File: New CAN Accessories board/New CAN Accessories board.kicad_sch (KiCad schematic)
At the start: 22 parts, among them J10 39301040, J11 ATF13-2P-BM03, J12 Conn_01x02_Pin, J9 39301060, T1 MCP2562FD-E_SN, U1 NUCLEO_L432KC

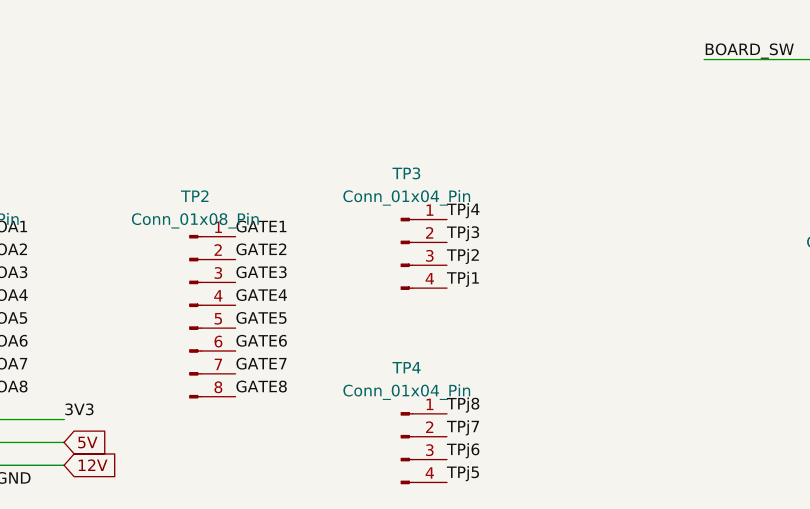
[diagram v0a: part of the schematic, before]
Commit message: added labellling changes noted in design review
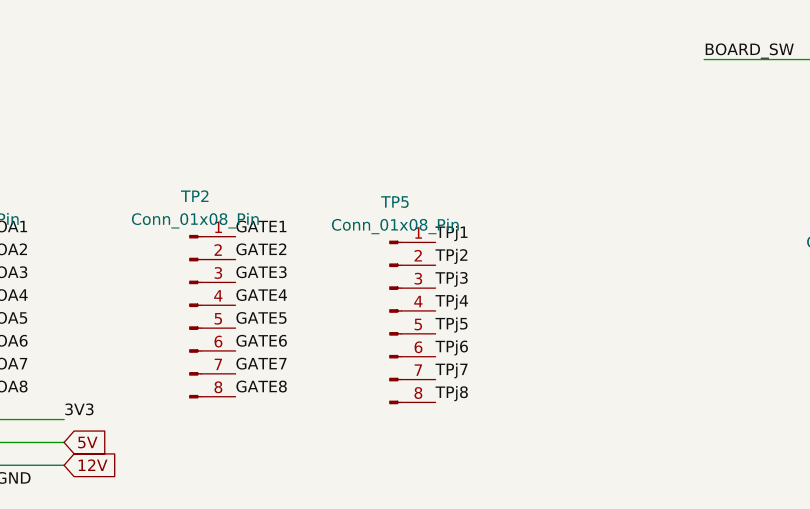
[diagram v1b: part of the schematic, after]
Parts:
- removed TP3, TP4: Conn_01x04_Pin, Connector_PinHeader_2.54mm:PinHeader_1x04_P2.54mm_Vertical, symbol Connector:Conn_01x04_Pin
- added TP5: Conn_01x08_Pin, Connector_PinHeader_2.54mm:PinHeader_1x08_P2.54mm_Vertical, symbol Connector:Conn_01x08_Pin
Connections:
- net TPj1: now also TP5.1 (Pin_1)
- net TPj2: now also TP5.2 (Pin_2)
- net TPj3: now also TP5.3 (Pin_3)
- net TPj4: now also TP5.4 (Pin_4)
- net TPj5: now also TP5.5 (Pin_5)
- net TPj6: now also TP5.6 (Pin_6)
- net TPj7: now also TP5.7 (Pin_7)
- net TPj8: now also TP5.8 (Pin_8)
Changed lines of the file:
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@@
 		)
 	)
-	(label "TPj1"
-		(at 87.63 166.37 0)
-		(effects
-			(font
-				(size 1.27 1.27)
-			)
-			(justify left bottom)
-		)
-	)
 	(label "GATE6"
 		(at 64.135 173.355 0)
@@
 		)
 	)
-	(label "TPj3"
-		(at 87.63 161.29 0)
-		(effects
-			(font
-				(size 1.27 1.27)
-			)
-			(justify left bottom)
-		)
-	)
-	(label "TPj5"
-		(at 87.63 187.96 0)
-		(effects
-			(font
-				(size 1.27 1.27)
-			)
-			(justify left bottom)
-		)
-	)
 	(label "3V3"
 		(at 97.79 106.68 0)
@@
 		)
 	)
-	(label "TPj2"
-		(at 87.63 163.83 0)
-		(effects
-			(font
-				(size 1.27 1.27)
-			)
-			(justify left bottom)
-		)
-	)
 	(label "STBY"
 		(at 46.99 71.12 0)
@@
 		)
 	)
-	(label "TPj7"
-		(at 87.63 182.88 0)
+	(label "OA2"
+		(at 37.465 163.195 0)
 		(effects
 			(font
@@
 		)
 	)
-	(label "OA2"
-		(at 37.465 163.195 0)
+	(label "GATE7"
+		(at 46.99 53.34 0)
 		(effects
 			(font
@@
 		)
 	)
-	(label "GATE7"
-		(at 46.99 53.34 0)
+	(label "TPj7"
+		(at 86.36 176.53 0)
 		(effects
 			(font
@@
 		)
 	)
-	(label "TPj4"
-		(at 87.63 158.75 0)
+	(label "OA4"
+		(at 201.93 39.37 0)
 		(effects
 			(font
@@
 		)
 	)
-	(label "OA4"
-		(at 201.93 39.37 0)
+	(label "CANH"
+		(at 172.72 80.01 0)
 		(effects
 			(font
@@
 		)
 	)
-	(label "CANH"
-		(at 172.72 80.01 0)
+	(label "OA7"
+		(at 95.25 53.34 0)
 		(effects
 			(font
@@
 		)
 	)
-	(label "OA7"
-		(at 95.25 53.34 0)
+	(label "TPj4"
+		(at 86.36 168.91 0)
 		(effects
 			(font
@@
 		)
 	)
-	(label "TPj8"
-		(at 87.63 180.34 0)
-		(effects
-			(font
-				(size 1.27 1.27)
-			)
-			(justify left bottom)
-		)
-	)
 	(label "3V3"
 		(at 116.84 124.46 0)
@@
 		)
 	)
-	(label "TPj6"
-		(at 87.63 185.42 0)
+	(label "OA6"
+		(at 37.465 173.355 0)
 		(effects
 			(font
@@
 		)
 	)
-	(label "OA6"
-		(at 37.465 173.355 0)
+	(label "TPj2"
+		(at 86.36 163.83 0)
 		(effects
 			(font
@@
 		)
 	)
+	(label "TPj8"
+		(at 86.36 179.07 0)
+		(effects
+			(font
+				(size 1.27 1.27)
+			)
+			(justify left bottom)
+		)
+	)
 	(label "GATE5"
 		(at 110.49 54.61 180)
@@
 		)
 	)
+	(label "TPj1"
+		(at 86.36 161.29 0)
+		(effects
+			(font
+				(size 1.27 1.27)
+			)
+			(justify left bottom)
+		)
+	)
 	(label "OA5"
 		(at 95.25 58.42 0)
@@
 		)
 	)
+	(label "TPj5"
+		(at 86.36 171.45 0)
+		(effects
+			(font
+				(size 1.27 1.27)
+			)
+			(justify left bottom)
+		)
+	)
 	(label "CANRX"
 		(at 35.56 106.68 0)
@@
 		)
 	)
+	(label "TPj3"
+		(at 86.36 166.37 0)
+		(effects
+			(font
+				(size 1.27 1.27)
+			)
+			(justify left bottom)
+		)
+	)
 	(label "OA1"
 		(at 37.465 160.655 0)
@@
 		)
 	)
+	(label "TPj6"
+		(at 86.36 173.99 0)
+		(effects
+			(font
+				(size 1.27 1.27)
+			)
+			(justify left bottom)
+		)
+	)
 	(label "OA7"
 		(at 37.465 175.895 0)
@@
 	)
 	(symbol
-		(lib_id "Connector:Conn_01x04_Pin")
-		(at 82.55 182.88 0)
-		(unit 1)
-		(exclude_from_sim no)
-		(in_bom yes)
-		(on_board yes)
-		(dnp no)
-		(fields_autoplaced yes)
-		(property "Reference" "TP4"
-			(at 83.185 175.26 0)
-			(effects
-				(font
-					(size 1.27 1.27)
-				)
-			)
-		)
-		(property "Value" "Conn_01x04_Pin"
-			(at 83.185 177.8 0)
-			(effects
-				(font
-					(size 1.27 1.27)
-				)
-			)
-		)
-		(property "Footprint" "Connector_PinHeader_2.54mm:PinHeader_1x04_P2.54mm_Vertical"
-			(at 82.55 182.88 0)
-			(effects
-				(font
-					(size 1.27 1.27)
-				)
-				(hide yes)
-			)
-		)
-		(property "Datasheet" "~"
-			(at 82.55 182.88 0)
-			(effects
-				(font
-					(size 1.27 1.27)
-				)
-				(hide yes)
-			)
-		)
-		(property "Description" "Generic connector, single row, 01x04, script generated"
-			(at 82.55 182.88 0)
-			(effects
-				(font
-					(size 1.27 1.27)
-				)
-				(hide yes)
-			)
-		)
-		(property "Purpose" ""
-			(at 82.55 182.88 0)
-			(effects
-				(font
-					(size 1.27 1.27)
-				)
-			)
-		)
-		(pin "3"
-		)
-		(pin "1"
-		)
-		(pin "2"
-		)
-		(pin "4"
-		)
-		(instances
-			(project "New CAN Accessories board"
-				(path "/88340f43-3f46-45a6-9393-130e00dc3071"
-					(reference "TP4")
-					(unit 1)
-				)
-			)
-		)
-	)
-	(symbol
 		(lib_id "Device:R")
 		(at 167.64 146.05 0)
@@
 	)
 	(symbol
+		(lib_id "Connector:Conn_01x08_Pin")
+		(at 81.28 168.91 0)
+		(unit 1)
+		(exclude_from_sim no)
+		(in_bom yes)
+		(on_board yes)
+		(dnp no)
+		(fields_autoplaced yes)
+		(property "Reference" "TP5"
+			(at 81.915 156.845 0)
+			(effects
+				(font
+					(size 1.27 1.27)
+				)
+			)
+		)
+		(property "Value" "Conn_01x08_Pin"
+			(at 81.915 159.385 0)
+			(effects
+				(font
+					(size 1.27 1.27)
+				)
+			)
+		)
+		(property "Footprint" "Connector_PinHeader_2.54mm:PinHeader_1x08_P2.54mm_Vertical"
+			(at 81.28 168.91 0)
+			(effects
+				(font
+					(size 1.27 1.27)
+				)
+				(hide yes)
+			)
+		)
+		(property "Datasheet" "~"
+			(at 81.28 168.91 0)
+			(effects
+				(font
+					(size 1.27 1.27)
+				)
+				(hide yes)
+			)
+		)
+		(property "Description" "Generic connector, single row, 01x08, script generated"
+			(at 81.28 168.91 0)
+			(effects
+				(font
+					(size 1.27 1.27)
+				)
+				(hide yes)
+			)
+		)
+		(property "Purpose" ""
+			(at 81.28 168.91 0)
+			(effects
+				(font
+					(size 1.27 1.27)
+				)
+			)
+		)
+		(pin "4"
+		)
+		(pin "6"
+		)
+		(pin "7"
+		)
+		(pin "1"
+		)
+		(pin "2"
+		)
+		(pin "5"
+		)
+		(pin "3"
+		)
+		(pin "8"
+		)
+		(instances
+			(project "New CAN Accessories board"
+				(path "/88340f43-3f46-45a6-9393-130e00dc3071"
+					(reference "TP5")
+					(unit 1)
+				)
+			)
+		)
+	)
+	(symbol
 		(lib_id "Switch:SW_DPDT_x2")
 		(at 172.72 124.46 0)
@@
 					(unit 1)
 				)
-			)
-		)
-	)
-	(symbol
-		(lib_id "Connector:Conn_01x04_Pin")
-		(at 82.55 161.29 0)
-		(unit 1)
-		(exclude_from_sim no)
-		(in_bom yes)
-		(on_board yes)
-		(dnp no)
-		(fields_autoplaced yes)
-		(property "Reference" "TP3"
-			(at 83.185 153.67 0)
-			(effects
-				(font
-					(size 1.27 1.27)
-				)
-			)
-		)
-		(property "Value" "Conn_01x04_Pin"
-			(at 83.185 156.21 0)
-			(effects
-				(font
-					(size 1.27 1.27)
-				)
-			)
-		)
-		(property "Footprint" "Connector_PinHeader_2.54mm:PinHeader_1x04_P2.54mm_Vertical"
-			(at 82.55 161.29 0)
-			(effects
-				(font
-					(size 1.27 1.27)
-				)
-				(hide yes)
-			)
-		)
-		(property "Datasheet" "~"
-			(at 82.55 161.29 0)
-			(effects
-				(font
-					(size 1.27 1.27)
-				)
-				(hide yes)
-			)
-		)
-		(property "Description" "Generic connector, single row, 01x04, script generated"
-			(at 82.55 161.29 0)
-			(effects
-				(font
-					(size 1.27 1.27)
-				)
-				(hide yes)
-			)
-		)
-		(property "Purpose" ""
-			(at 82.55 161.29 0)
-			(effects
-				(font
-					(size 1.27 1.27)
-				)
-			)
-		)
-		(pin "3"
-		)
-		(pin "1"
-		)
-		(pin "2"
-		)
-		(pin "4"
-		)
-		(instances
-			(project ""
-				(path "/88340f43-3f46-45a6-9393-130e00dc3071"
-					(reference "TP3")
-					(unit 1)
-				)

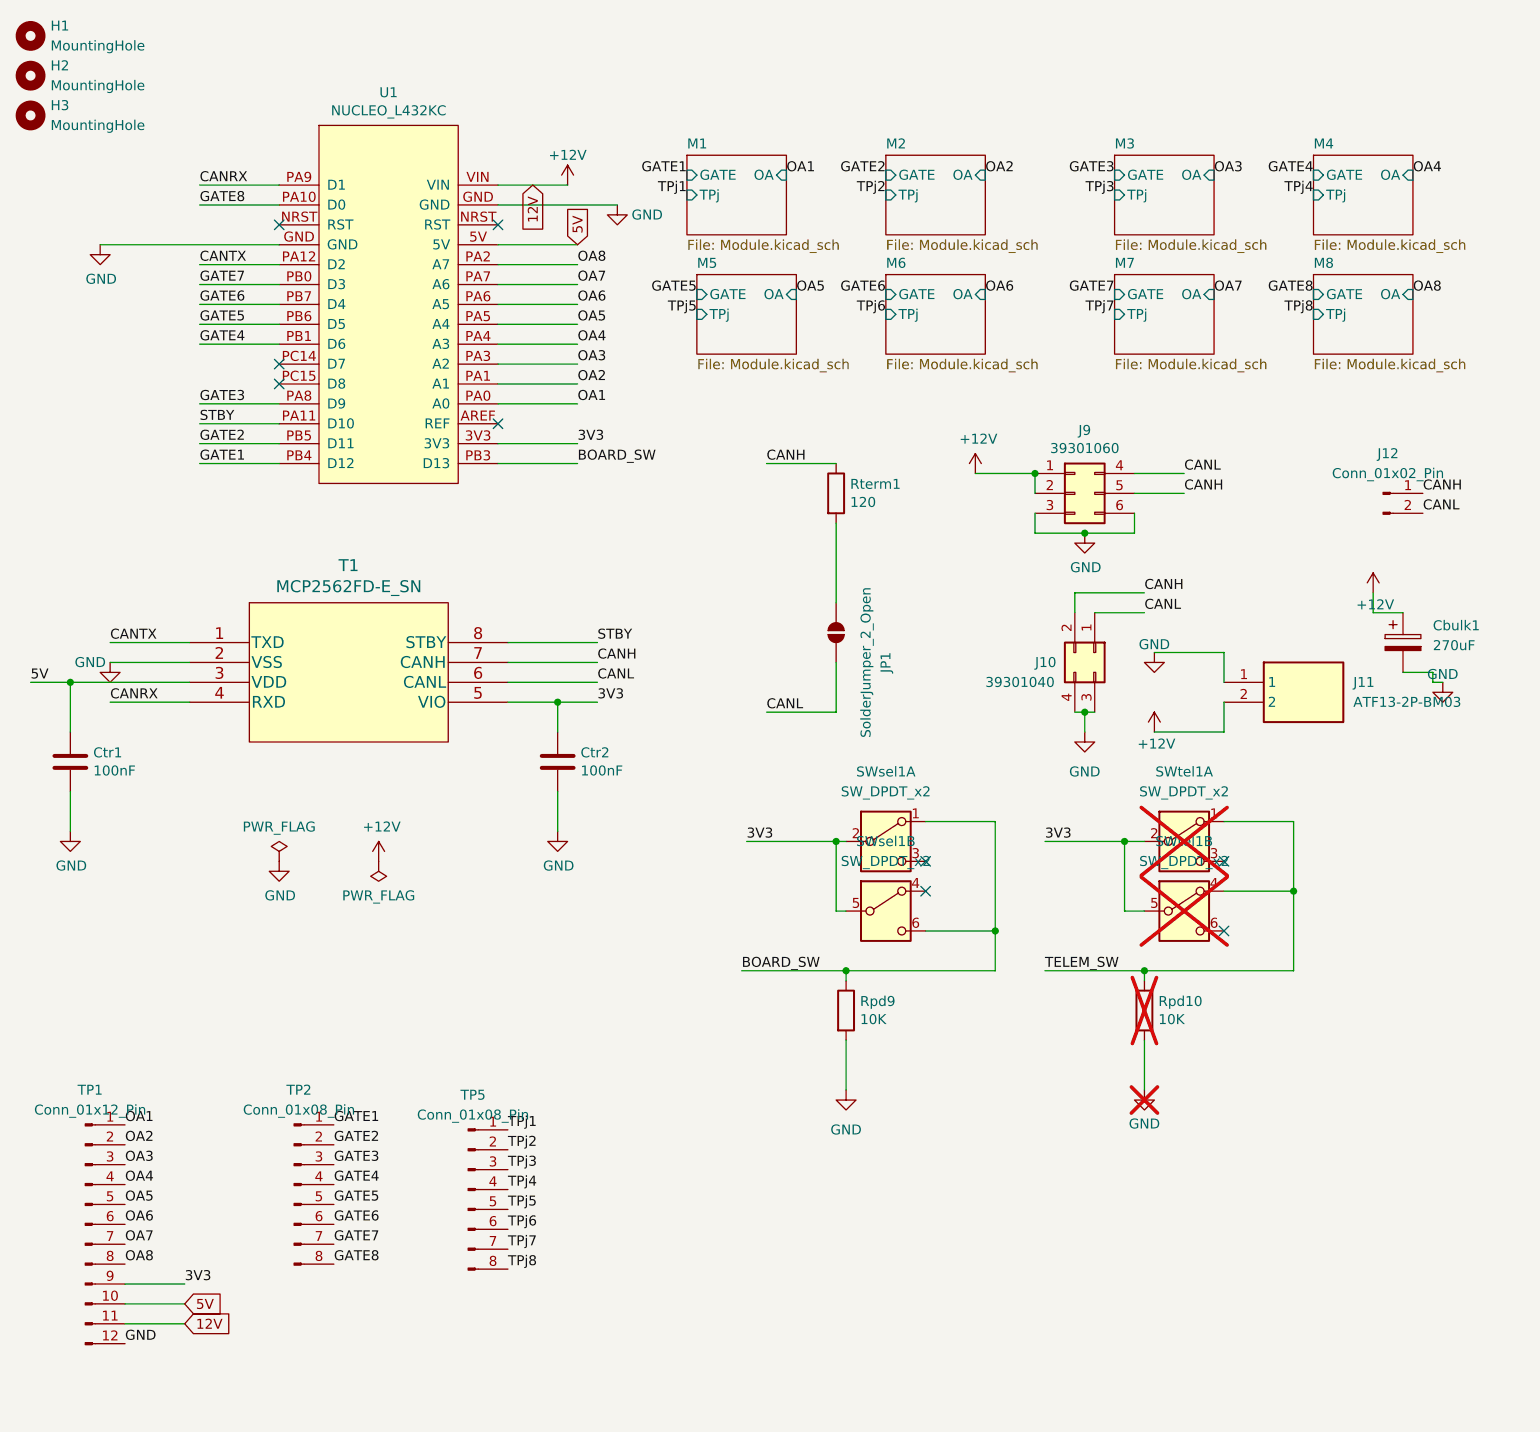
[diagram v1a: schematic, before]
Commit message: started making drain test point changes
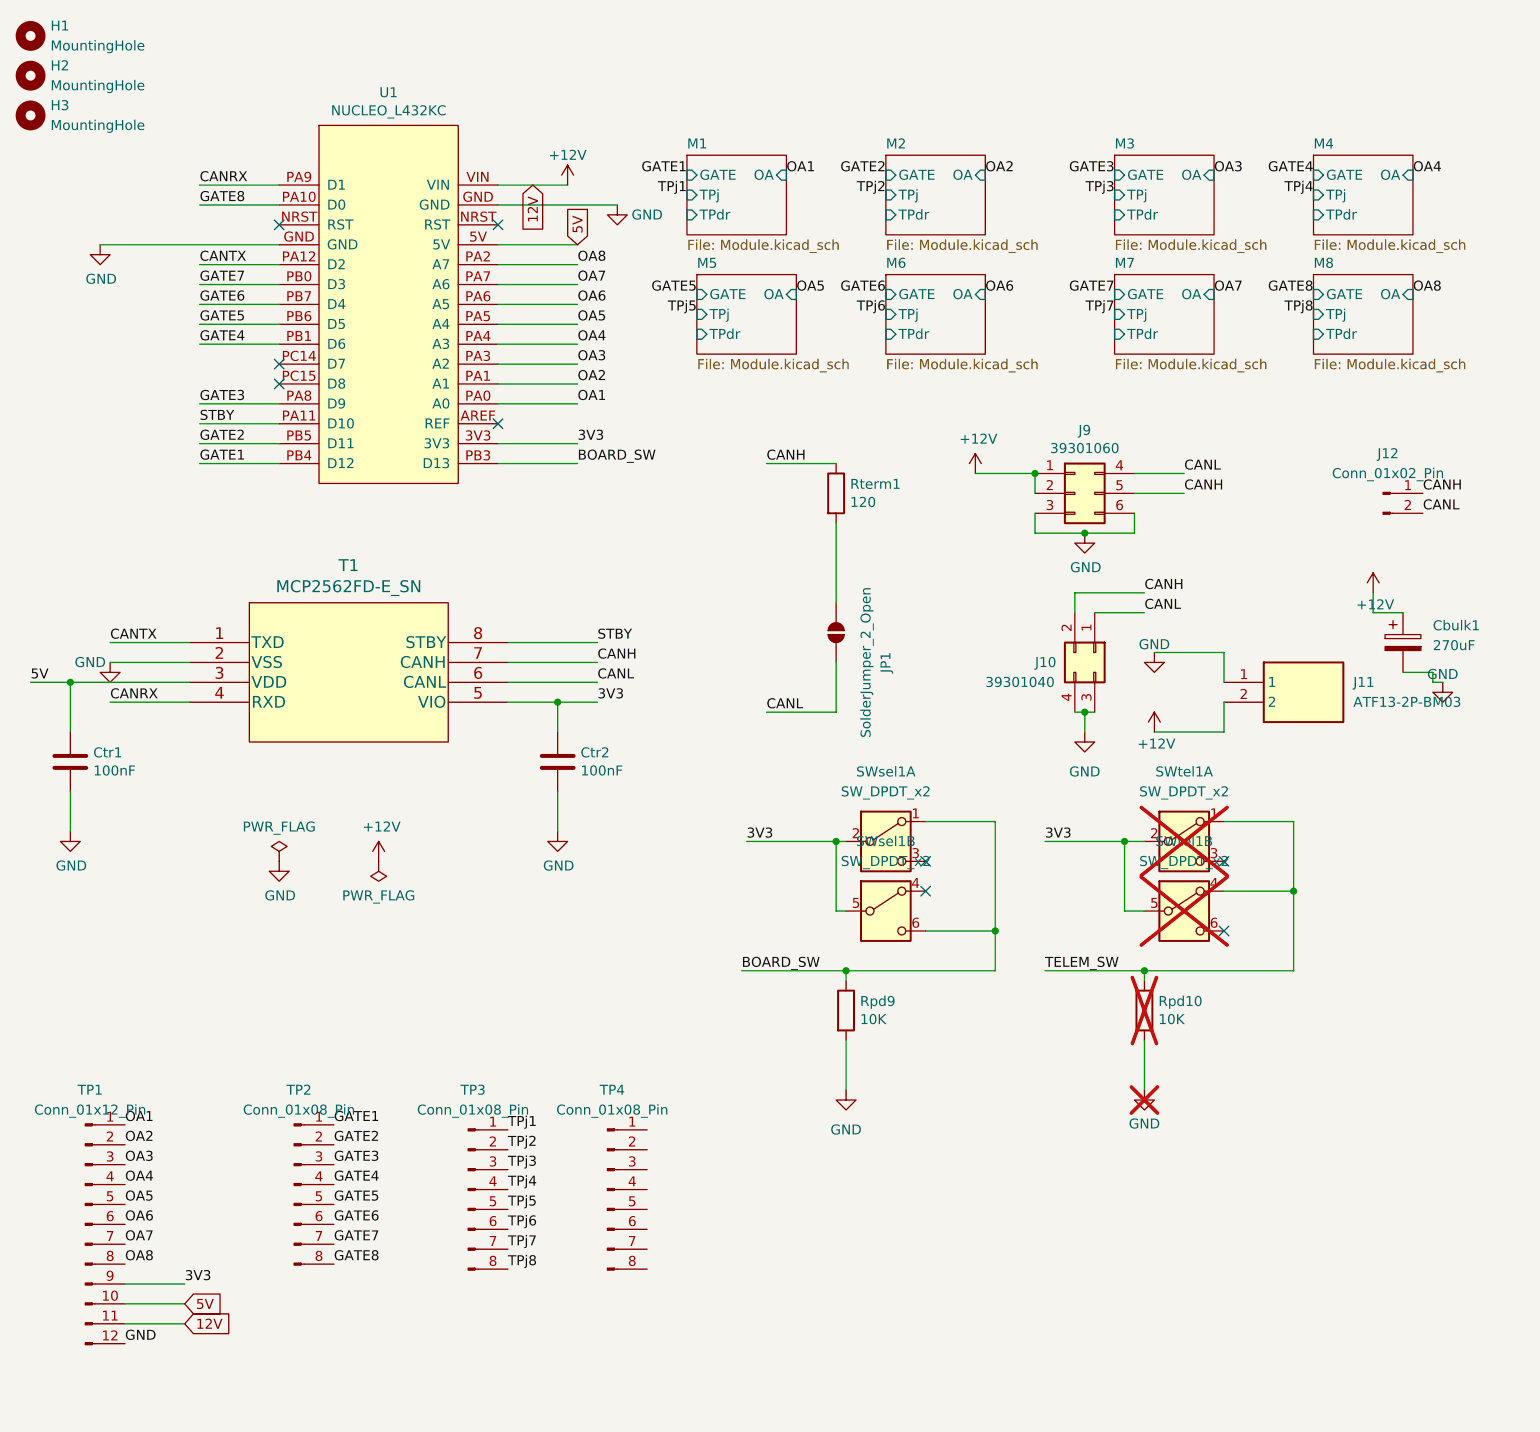
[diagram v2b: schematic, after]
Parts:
- added TP4: Conn_01x08_Pin, Connector_PinHeader_2.54mm:PinHeader_1x08_P2.54mm_Vertical, symbol Connector:Conn_01x08_Pin
- renumbered TP5 to TP3
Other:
- sheet M1 ports: added TPdr; removed none
- sheet M2 ports: added TPdr; removed none
- sheet M3 ports: added TPdr; removed none
- sheet M4 ports: added TPdr; removed none
- sheet M5 ports: added TPdr; removed none
- sheet M6 ports: added TPdr; removed none
- sheet M7 ports: added TPdr; removed none
- sheet M8 ports: added TPdr; removed none
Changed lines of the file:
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@@
+	)
+	(symbol
+		(lib_id "Connector:Conn_01x08_Pin")
+		(at 99.06 168.91 0)
+		(unit 1)
+		(exclude_from_sim no)
+		(in_bom yes)
+		(on_board yes)
+		(dnp no)
+		(fields_autoplaced yes)
+		(property "Reference" "TP4"
+			(at 99.695 156.21 0)
+			(effects
+				(font
+					(size 1.27 1.27)
+				)
+			)
+		)
+		(property "Value" "Conn_01x08_Pin"
+			(at 99.695 158.75 0)
+			(effects
+				(font
+					(size 1.27 1.27)
+				)
+			)
+		)
+		(property "Footprint" "Connector_PinHeader_2.54mm:PinHeader_1x08_P2.54mm_Vertical"
+			(at 99.06 168.91 0)
+			(effects
+				(font
+					(size 1.27 1.27)
+				)
+				(hide yes)
+			)
+		)
+		(property "Datasheet" "~"
+			(at 99.06 168.91 0)
+			(effects
+				(font
+					(size 1.27 1.27)
+				)
+				(hide yes)
+			)
+		)
+		(property "Description" "Generic connector, single row, 01x08, script generated"
+			(at 99.06 168.91 0)
+			(effects
+				(font
+					(size 1.27 1.27)
+				)
+				(hide yes)
+			)
+		)
+		(property "Purpose" ""
+			(at 99.06 168.91 0)
+			(effects
+				(font
+					(size 1.27 1.27)
+				)
+			)
+		)
+		(pin "4"
+		)
+		(pin "6"
+		)
+		(pin "7"
+		)
+		(pin "1"
+		)
+		(pin "2"
+		)
+		(pin "5"
+		)
+		(pin "3"
+		)
+		(pin "8"
+		)
+		(instances
+			(project "New CAN Accessories board"
+				(path "/88340f43-3f46-45a6-9393-130e00dc3071"
+					(reference "TP4")
+					(unit 1)
+				)
+			)
+		)
 	)
 	(symbol
@@
 		(dnp no)
 		(fields_autoplaced yes)
-		(property "Reference" "TP5"
-			(at 81.915 156.845 0)
+		(property "Reference" "TP3"
+			(at 81.915 156.21 0)
 			(effects
 				(font
@@
 		)
 		(property "Value" "Conn_01x08_Pin"
-			(at 81.915 159.385 0)
+			(at 81.915 158.75 0)
 			(effects
 				(font
@@
 			(project "New CAN Accessories board"
 				(path "/88340f43-3f46-45a6-9393-130e00dc3071"
-					(reference "TP5")
+					(reference "TP3")
 					(unit 1)
 				)
@@
 			)
 		)
+		(pin "TPdr" input
+			(at 163.83 44.45 180)
+			(effects
+				(font
+					(size 1.27 1.27)
+				)
+				(justify left)
+			)
+		)
 		(instances
 			(project "New CAN Accessories board"
@@
 			)
 		)
+		(pin "TPdr" input
+			(at 134.62 44.45 180)
+			(effects
+				(font
+					(size 1.27 1.27)
+				)
+				(justify left)
+			)
+		)
 		(instances
 			(project "New CAN Accessories board"
@@
 			)
 		)
+		(pin "TPdr" input
+			(at 189.23 59.69 180)
+			(effects
+				(font
+					(size 1.27 1.27)
+				)
+				(justify left)
+			)
+		)
 		(instances
 			(project "New CAN Accessories board"
@@
 			)
 		)
+		(pin "TPdr" input
+			(at 163.83 59.69 180)
+			(effects
+				(font
+					(size 1.27 1.27)
+				)
+				(justify left)
+			)
+		)
 		(instances
 			(project "New CAN Accessories board"
@@
 			)
 		)
+		(pin "TPdr" input
+			(at 134.62 59.69 180)
+			(effects
+				(font
+					(size 1.27 1.27)
+				)
+				(justify left)
+			)
+		)
 		(instances
 			(project "New CAN Accessories board"
@@
 			)
 		)
+		(pin "TPdr" input
+			(at 189.23 44.45 180)
+			(effects
+				(font
+					(size 1.27 1.27)
+				)
+				(justify left)
+			)
+		)
 		(instances
 			(project "New CAN Accessories board"
@@
 			)
 		)
+		(pin "TPdr" input
+			(at 110.49 59.69 180)
+			(effects
+				(font
+					(size 1.27 1.27)
+				)
+				(justify left)
+			)
+		)
 		(instances
 			(project "New CAN Accessories board"
@@
 			(effects
 				(font
+					(size 1.27 1.27)
+				)
+				(justify left)
+			)
+		)
+		(pin "TPdr" input
+			(at 109.22 44.45 180)
+			(effects
+				(font
